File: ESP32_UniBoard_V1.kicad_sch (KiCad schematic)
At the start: 30 parts, among them J1 USB_C_Receptacle_USB2.0, J2 Conn_01x06_Socket, J3 Hirose DF40C, SW1 SW_Push, SW2 SW_Push, U1 ESP32-S3-WROOM-1, U2 AZ1117-3.3, U3 USBLC6-2SC6

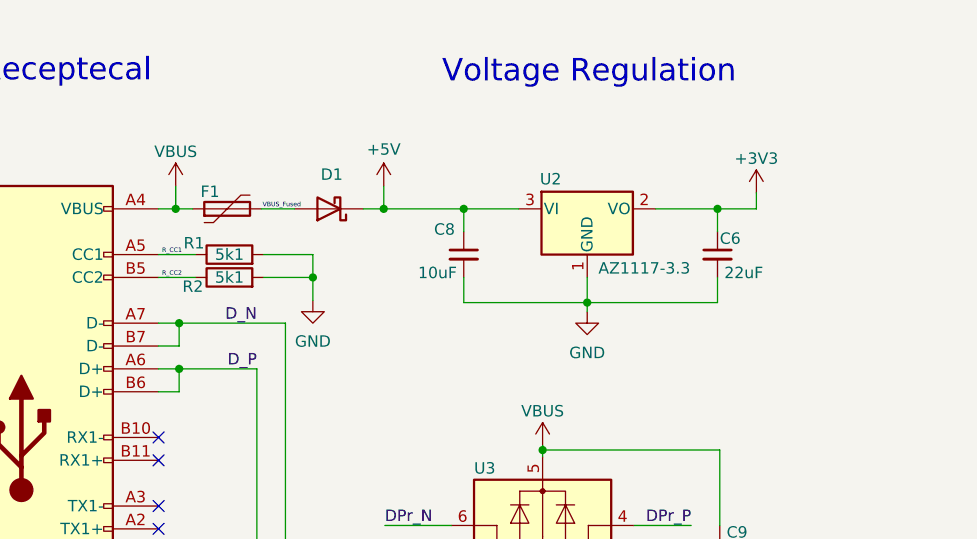
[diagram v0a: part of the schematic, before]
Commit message: PCB changed to 4 Layer WIP
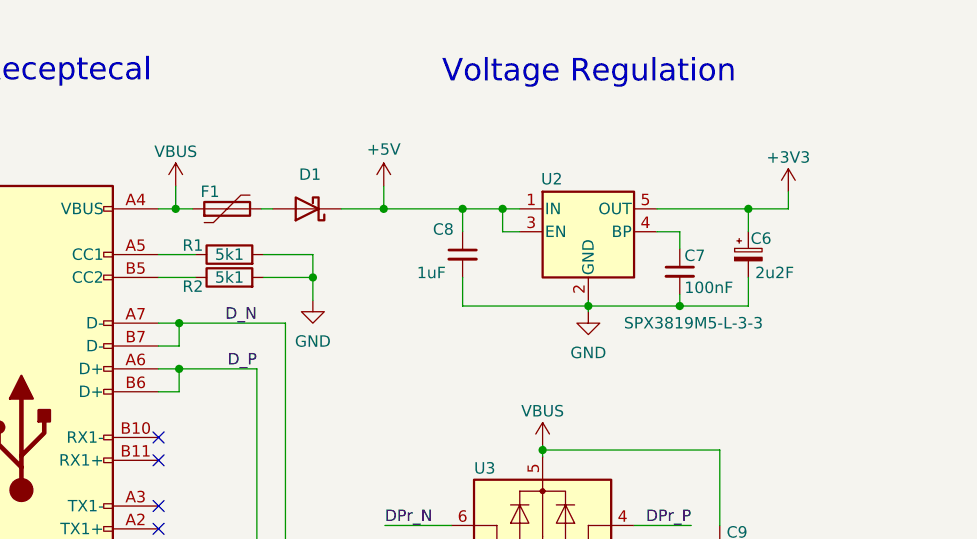
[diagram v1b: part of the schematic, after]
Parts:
- removed U2: AZ1117-3.3, Package_TO_SOT_SMD:SOT-223-3_TabPin2, symbol Regulator_Linear:AZ1117-3.3
- added C7: 100nF, Capacitor_SMD:C_0603_1608Metric_Pad1.08x0.95mm_HandSolder, symbol Device:C_Small
- added U2: SPX3819M5-L-3-3, Package_TO_SOT_SMD:SOT-23-5, symbol Regulator_Linear:SPX3819M5-L-3-3
- C1, C2, C3, C4, C5, C9: footprint Capacitor_SMD:C_0603_1608Metric -> Capacitor_SMD:C_0603_1608Metric_Pad1.08x0.95mm_HandSolder
- C6: value 22uF -> 2u2F; footprint Capacitor_SMD:C_0805_2012Metric -> Capacitor_SMD:CP_Elec_4x5.4; symbol Device:C_Small -> Device:C_Polarized_Small
- C8: value 10uF -> 1uF; footprint Capacitor_SMD:C_0603_1608Metric -> Capacitor_SMD:C_0603_1608Metric_Pad1.08x0.95mm_HandSolder
- D1: footprint Diode_SMD:D_0603_1608Metric -> Diode_SMD:D_0603_1608Metric_Pad1.05x0.95mm_HandSolder
- D2, D3, D4: footprint LED_SMD:LED_0603_1608Metric -> LED_SMD:LED_0603_1608Metric_Pad1.05x0.95mm_HandSolder
- F1: footprint Fuse:Fuse_0805_2012Metric -> Fuse:Fuse_0805_2012Metric_Pad1.15x1.40mm_HandSolder
- R1, R2, R3, R4, R5, R6: footprint Resistor_SMD:R_0603_1608Metric -> Resistor_SMD:R_0603_1608Metric_Pad0.98x0.95mm_HandSolder
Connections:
- net +3V3: now also U2.5 (OUT)
- net +5V: now also U2.1 (IN), U2.3 (EN)
- net GND: now also C7.2, U2.2 (GND)
- net R_CC1: no longer names the net of J1.A5 (CC1), R1.1
- net R_CC2: no longer names the net of J1.B5 (CC2), R2.1
- net VBUS_Fused: no longer names the net of D1.2 (A), F1.2
- new net: C7.1, U2.4 (BP)
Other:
- moved on the sheet: D1
